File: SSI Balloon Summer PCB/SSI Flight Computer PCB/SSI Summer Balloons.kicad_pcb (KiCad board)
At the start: 4 copper layers, 77.5 x 61 mm, 111 parts, among them J1 Battery connector, J10 Conn_01x08, J2 Conn_01x02, J3 LoRa antenna, J5 SWDIO, J6 1040310811, J7 GPS antenna, J8 PT1000 Sensor, M1 MountingHole_3.2mm_M3, M2 MountingHole_3.2mm_M3, M3 MountingHole_3.2mm_M3, M4 MountingHole_3.2mm_M3, Q2 DMG2305UX-7, SW1 NRST, SW2 BOOT0, U11 TPS63070RNMR, U3 AP2112K-3.3TRG1, U7 STM32F411CEUx, Y1 ABM8W-12.0000MHZ-8-K1Z-T3

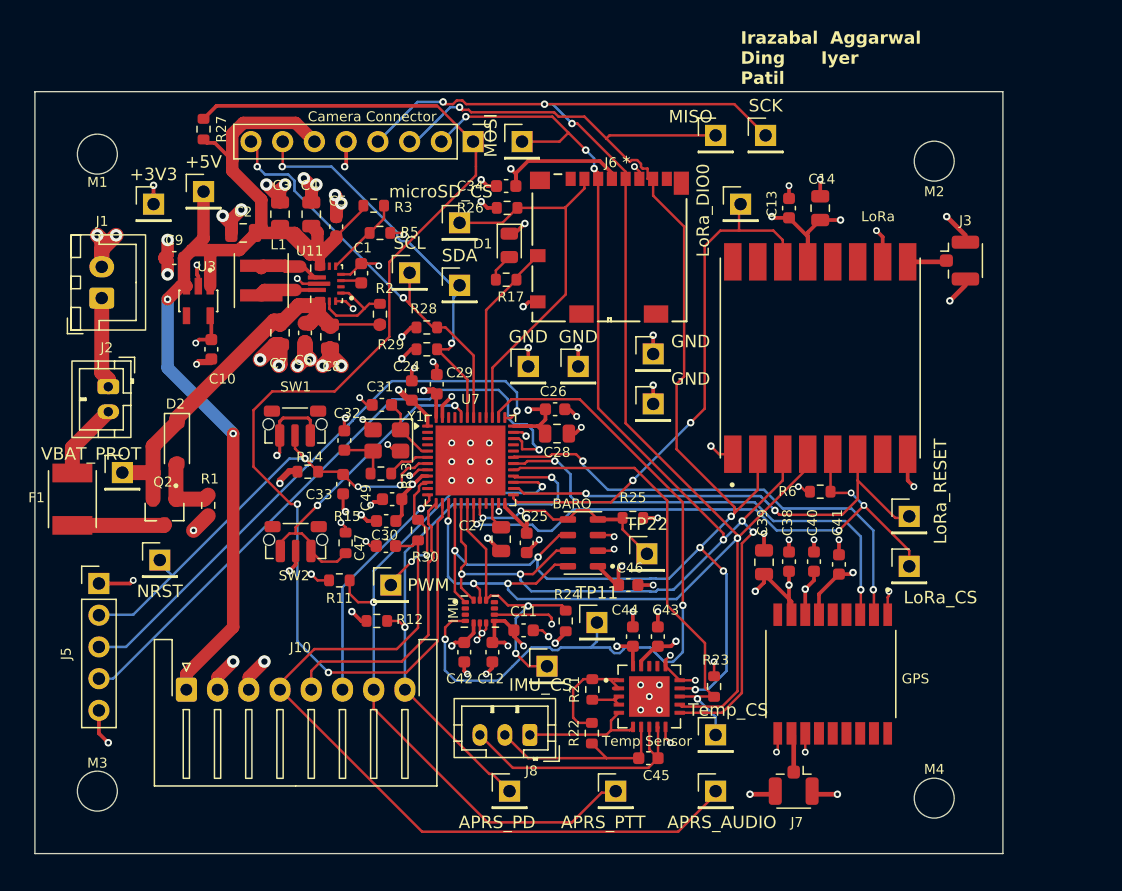
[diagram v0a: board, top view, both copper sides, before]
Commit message: Cleared space for microSD, organized SPI tracks
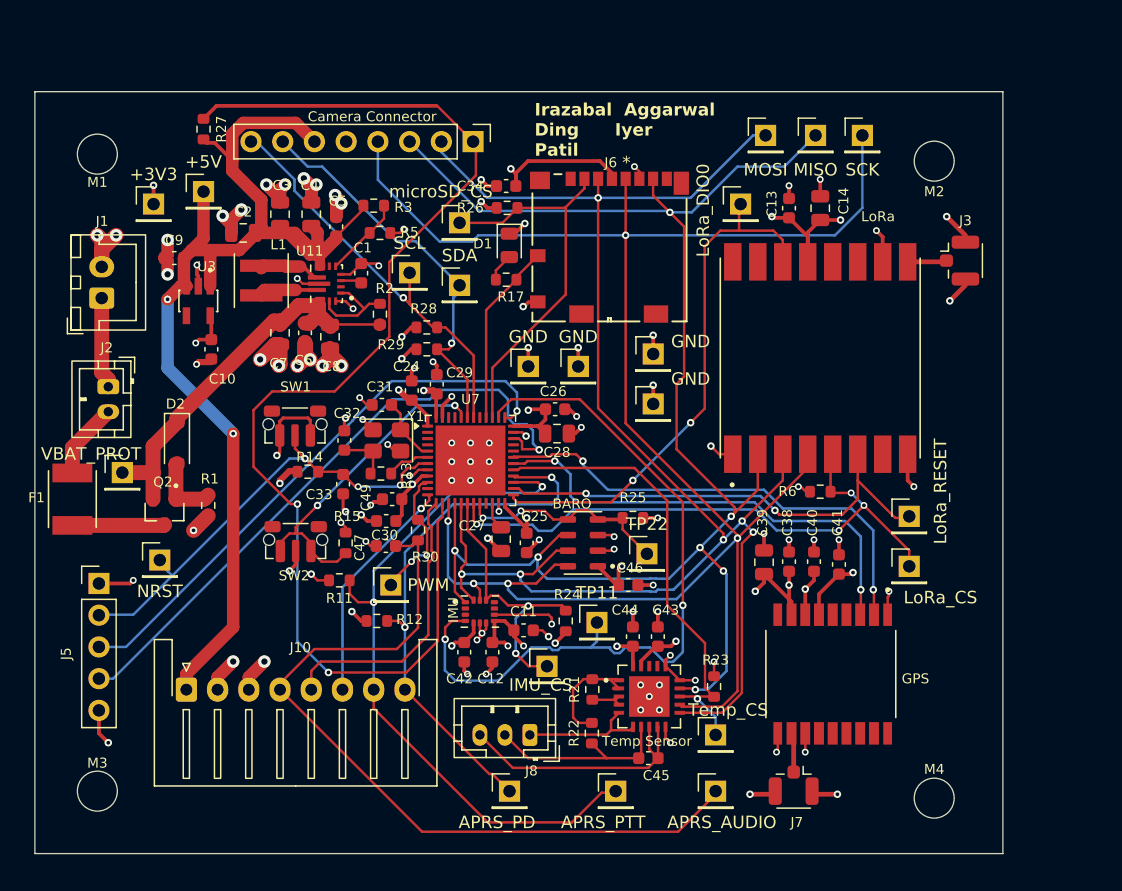
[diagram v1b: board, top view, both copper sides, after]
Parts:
- moved MOSI 19.5 mm to (158.5, 80.0)
- moved MISO 8.00 mm to (162.5, 80.0)
- moved SCK 7.75 mm to (166.2, 80.0)
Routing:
- net /MCU (STM)/MOSI: track 119.2 -> 129.0 mm, vias 8 -> 6
- net /MCU (STM)/SCK: track 141.1 -> 148.9 mm, vias 7 -> 5
- net /MCU (STM)/MISO: track 121.8 -> 126.5 mm
- net /MCU (STM)/SDA: track 35.2 -> 32.6 mm, vias 2 -> 1
- net GND: track 169.7 -> 167.9 mm, vias 100 -> 99
- net /MCU (STM)/SCL: track 34.2 -> 34.0 mm, vias 2 -> 1

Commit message: More silkscreen organization, combined some pinheaders
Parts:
- removed MISO, MOSI, SCK, SCL, SDA: Conn_01x01, Connector_PinHeader_2.54mm:PinHeader_1x01_P2.54mm_Vertical
- added J11: SPI, Connector_PinHeader_2.54mm:PinHeader_1x03_P2.54mm_Vertical, F.Cu at (164.8, 80.0)
- added J4: I2C, Connector_PinHeader_2.54mm:PinHeader_1x02_P2.54mm_Vertical, F.Cu at (130.5, 91.5)
- J1: value Battery connector -> BATT_CONN
- J9: renamed from Camera Connector; value Camera -> CAM_CONN
- TP1: renamed from +5V; value Conn_01x01 -> +5V
- TP10: renamed from NRST; value Conn_01x01 -> NRST
- TP11: value Conn_01x01 -> IMU_INT1
- TP12: renamed from LoRa_DIO0; value Conn_01x01 -> LoRa_DIO0
- TP13, TP3, TP5, TP8: renamed from GND; value Conn_01x01 -> GND
- TP14: renamed from APRS_PD; value Conn_01x01 -> APRS_PD
- TP15: renamed from APRS_PTT; value Conn_01x01 -> APRS_PT
- TP2: renamed from VBAT_PROT; value Conn_01x01 -> VBAT_PROT
- TP20: renamed from IMU_CS; value Conn_01x01 -> IMU_CS
- TP21: renamed from Temp_CS; value Conn_01x01 -> Temp_CS
- TP22: value Conn_01x01 -> BARO_CS
- TP23: renamed from LoRa_CS; value Conn_01x01 -> LoRa_CS
- TP24: renamed from microSD_CS; value Conn_01x01 -> microSD_CS
- TP25: renamed from LoRa_RESET; value Conn_01x01 -> LoRa_RESET
- TP4: renamed from +3V3; value Conn_01x01 -> +3V3
- TP6: renamed from APRS_AUDIO; value Conn_01x01 -> APRS_AUDIO
- TP7: renamed from PWM; value Conn_01x01 -> APRS_PWM
- U9: renamed from Temp Sensor
- moved TP1 1.35 mm to (113.0, 85.8)
- moved TP24 1.35 mm to (132.8, 87.5)
- moved TP2 1.12 mm to (106.5, 108.0)
- moved F1 0.50 mm to (102.5, 109.1)
- moved TP4 0.35 mm to (109.2, 85.8)
- renumbered LoRa to U1, BARO to U10, GPS to U8
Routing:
- net GND: track 167.9 -> 161.3 mm, vias 99 -> 95
- net +5V: track 92.3 -> 87.9 mm
- net +3V3: track 109.2 -> 104.8 mm, vias 33 -> 31
- net /MCU (STM)/SCK: track 148.9 -> 146.9 mm
- net /MCU (STM)/microSD_CS: track 31.2 -> 32.6 mm
- net /MCU (STM)/SDA: track 32.6 -> 33.9 mm
- net /MCU (STM)/MOSI: track 129.0 -> 130.3 mm
- net VBAT_PROT: track 32.7 -> 33.6 mm
- net /MCU (STM)/SCL: track 34.0 -> 34.9 mm, vias 1 -> 0
- net Net-(F1-Pad2): track 7.40 -> 7.90 mm

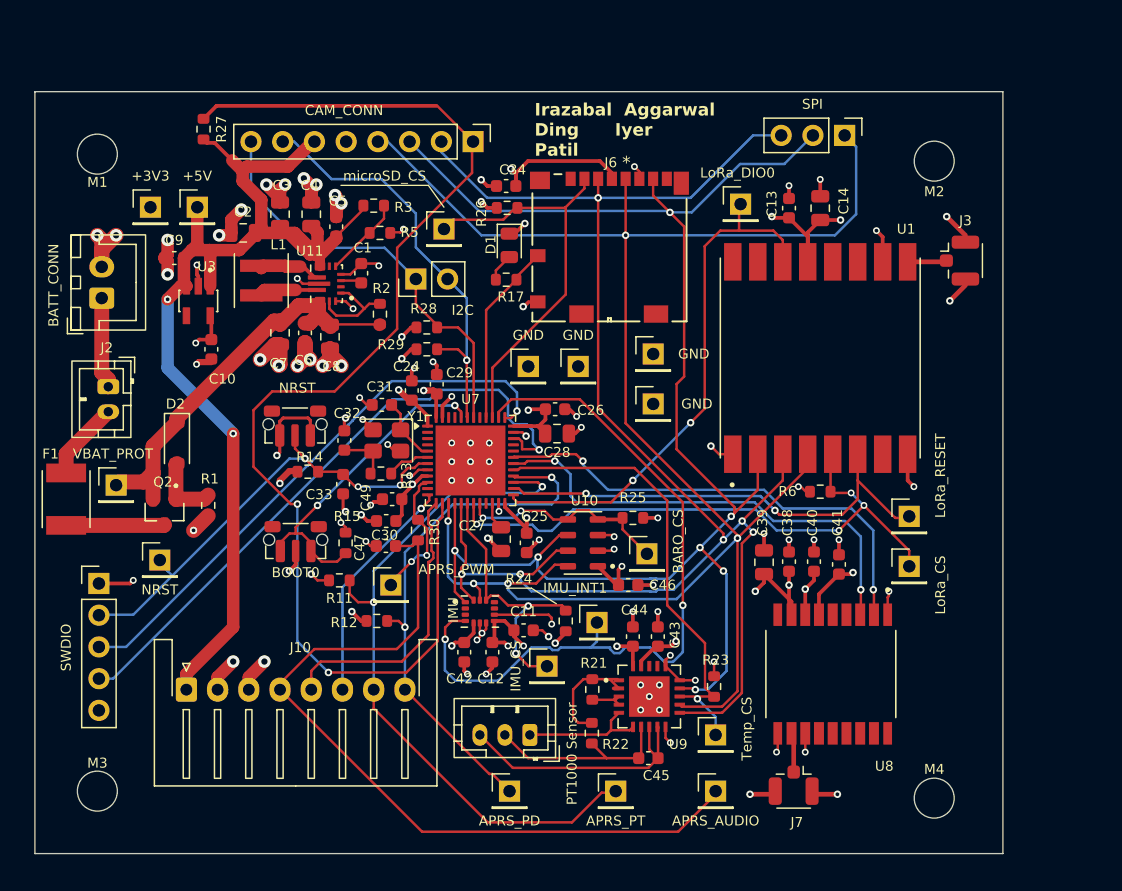
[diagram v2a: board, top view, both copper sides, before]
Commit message: Updated antenna connector
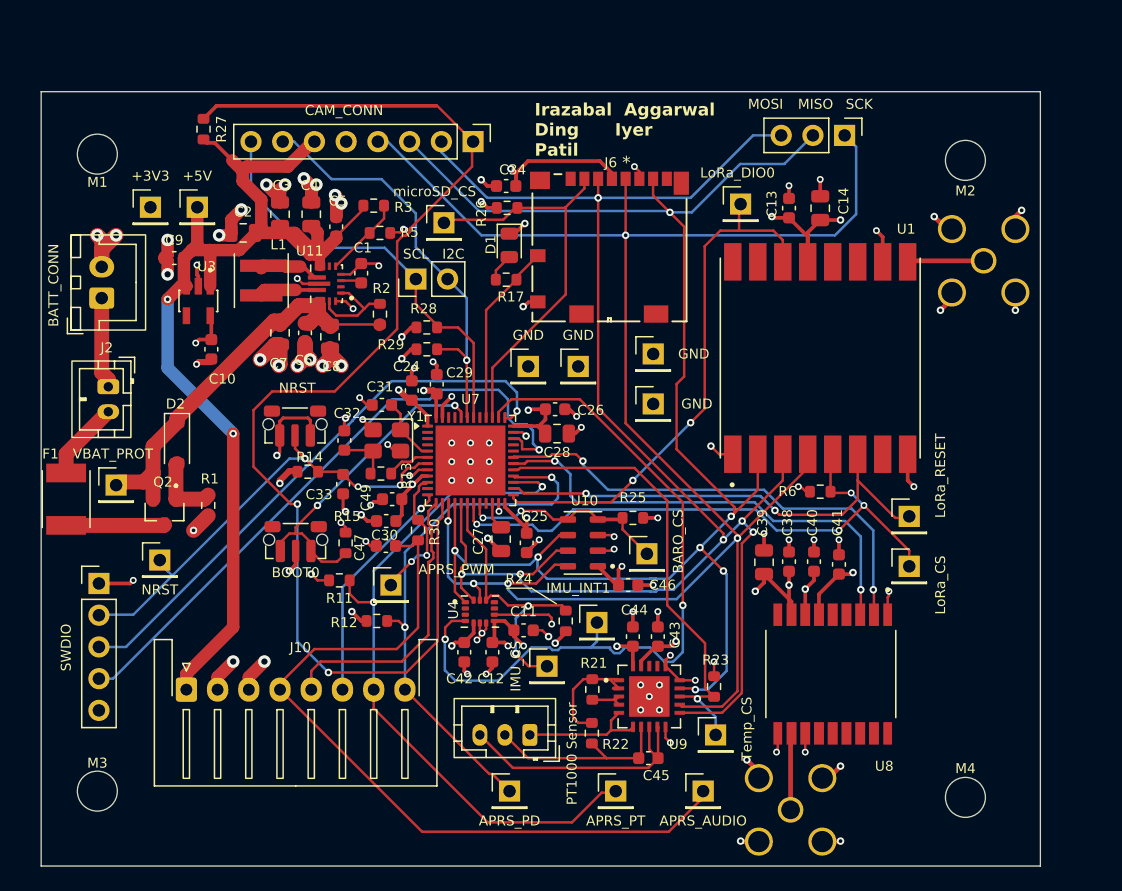
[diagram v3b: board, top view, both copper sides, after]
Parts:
- J3, J7: footprint Connector_Coaxial:U.FL_Hirose_U.FL-R-SMT-1_Vertical -> Connector_Coaxial:SMA_Amphenol_901-144_Vertical; moved to B.Cu
- moved M2 2.50 mm to (174.5, 82.0)
- moved M4 2.50 mm to (174.5, 133.0)
- moved J7 1.52 mm to (160.5, 134.0)
- moved J3 1.46 mm to (176.0, 90.0), turned to 180 degrees
- moved TP6 1.00 mm to (153.5, 132.5)
- moved TP24 0.50 mm to (132.8, 87.0)
- renumbered IMU to U4
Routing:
- net GND: track 161.3 -> 165.5 mm, vias 95 -> 99
- net Net-(J7-In): track 3.17 -> 6.40 mm
- net Net-(J3-In): track 3.14 -> 6.12 mm
- net /MCU (STM)/APRS_AUDIO: track 63.2 -> 62.5 mm
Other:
- board size 77.5 x 61 mm -> 80 x 62 mm
- board text added: "MISO"
- board text added: "MOSI"
- board text added: "SCK"
- board text added: "SCL"

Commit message: finished finding all parts on JLCPCB - finalizing BOM then order
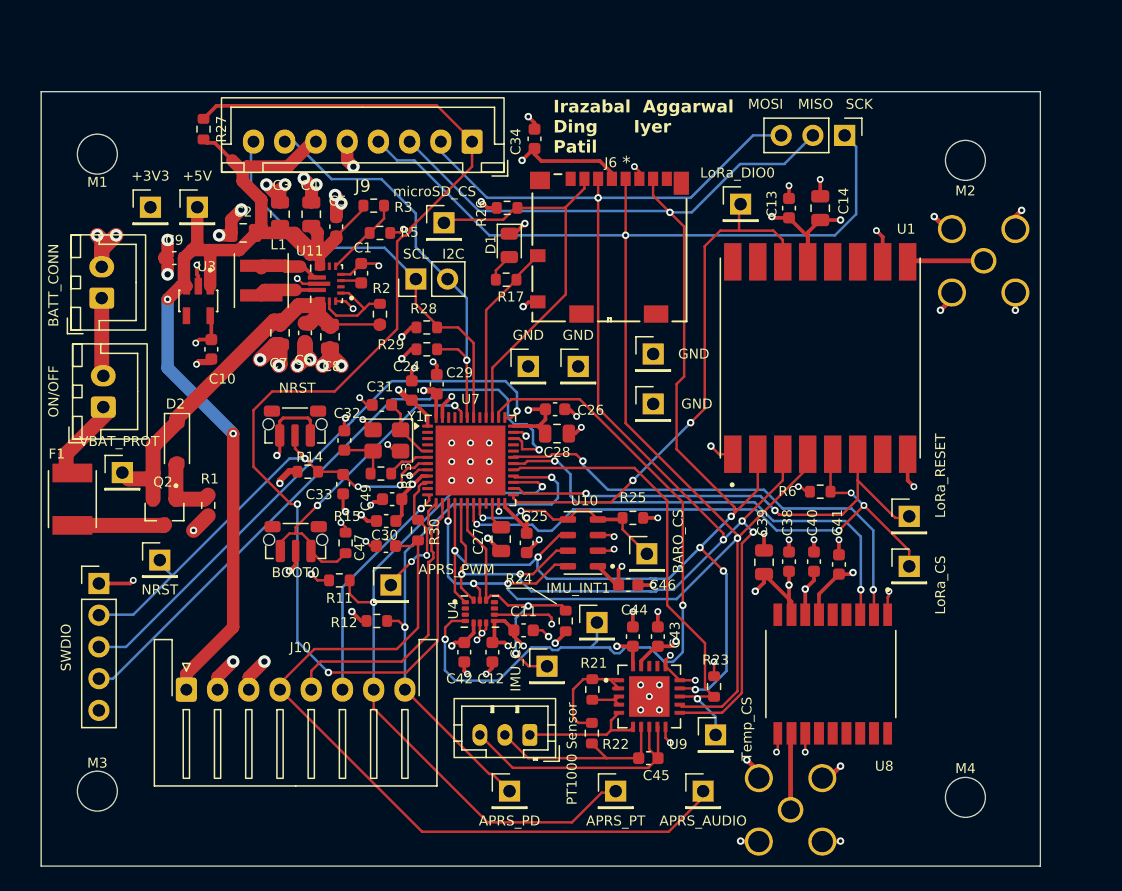
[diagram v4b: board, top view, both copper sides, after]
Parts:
- C1: value 100 nF -> 100nF
- C11, C33: value 0.1uF -> 100nF
- J2: footprint Connector_JST:JST_PH_B2B-PH-K_1x02_P2.00mm_Vertical -> Connector_JST:JST_XH_B2B-XH-A_1x02_P2.50mm_Vertical
- J9: footprint Connector_PinHeader_2.54mm:PinHeader_1x08_P2.54mm_Vertical -> Connector_JST:JST_XH_B8B-XH-A_1x08_P2.50mm_Vertical
- R17: value 330R -> 330
- moved C34 4.41 mm to (140.0, 80.3), turned to 90 degrees
- moved J2 1.67 mm to (105.5, 101.8), turned to 90 degrees
- moved TP2 1.12 mm to (107.0, 107.0)
- moved F1 0.50 mm to (103.0, 109.1)
- moved J9 0.08 mm to (135.0, 80.5), turned to 180 degrees
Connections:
- F1 pad 1: Net-(J2-Pin_2) -> Net-(J2-Pin_1)
- J2 pad 1: VBAT -> Net-(J2-Pin_1)
- J2 pad 2: Net-(J2-Pin_2) -> VBAT
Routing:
- net Net-(J2-Pin_1): track 0.00 -> 6.85 mm
- net Net-(J2-Pin_2): track 6.30 -> 0.00 mm
- net +3V3: track 104.8 -> 102.4 mm
- net GND: track 165.5 -> 167.5 mm, vias 99 -> 100
- net VBAT: track 7.32 -> 6.28 mm
- net /MCU (STM)/SDA: track 33.9 -> 34.9 mm
- net /MCU (STM)/SCK: track 146.9 -> 147.7 mm
- net VBAT_PROT: track 33.6 -> 32.9 mm
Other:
- board text added: "ON/OFF"

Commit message: PCB finally done i think and ready to order
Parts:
- removed R17: 330, Resistor_SMD:R_0603_1608Metric
- added C35: 1uF, Capacitor_SMD:C_0603_1608Metric, F.Cu at (153.0, 81.0)
- added R18: 330, Resistor_SMD:R_0603_1608Metric, F.Cu at (137.3, 93.3)
- added R31: 1k, Resistor_SMD:R_0603_1608Metric, F.Cu at (139.5, 118.0)
- R13: value R_EXT -> 0
- moved C34 1.24 mm to (139.0, 81.0)
- moved D1 1.13 mm to (137.5, 89.8)
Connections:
- U4 pad 9: GND -> Net-(U4-INT2/FSYNC/CLKIN)
- U7 pad 41: unconnected-(U7-PB5-Pad41) -> Net-(U7-PB5)
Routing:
- net Net-(U7-PB5): track 0.00 -> 9.18 mm
- net +3V3: track 102.4 -> 111.4 mm, vias 31 -> 32
- net GND: track 167.5 -> 164.4 mm, vias 100 -> 101
- net /MCU (STM)/IMU_CS: track 22.7 -> 25.0 mm
- net Net-(U4-INT2/FSYNC/CLKIN): track 0.00 -> 2.04 mm

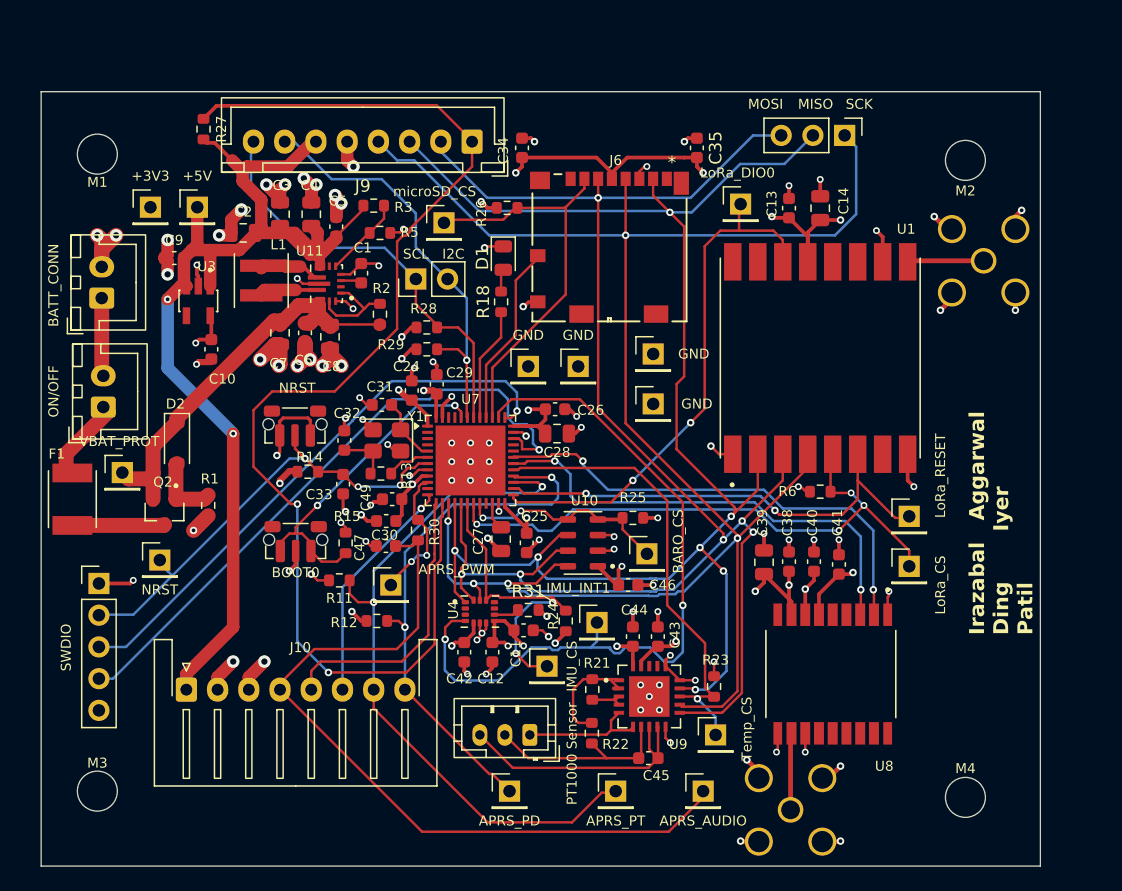
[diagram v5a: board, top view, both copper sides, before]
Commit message: Board done but we have a price crisis so might have to change things
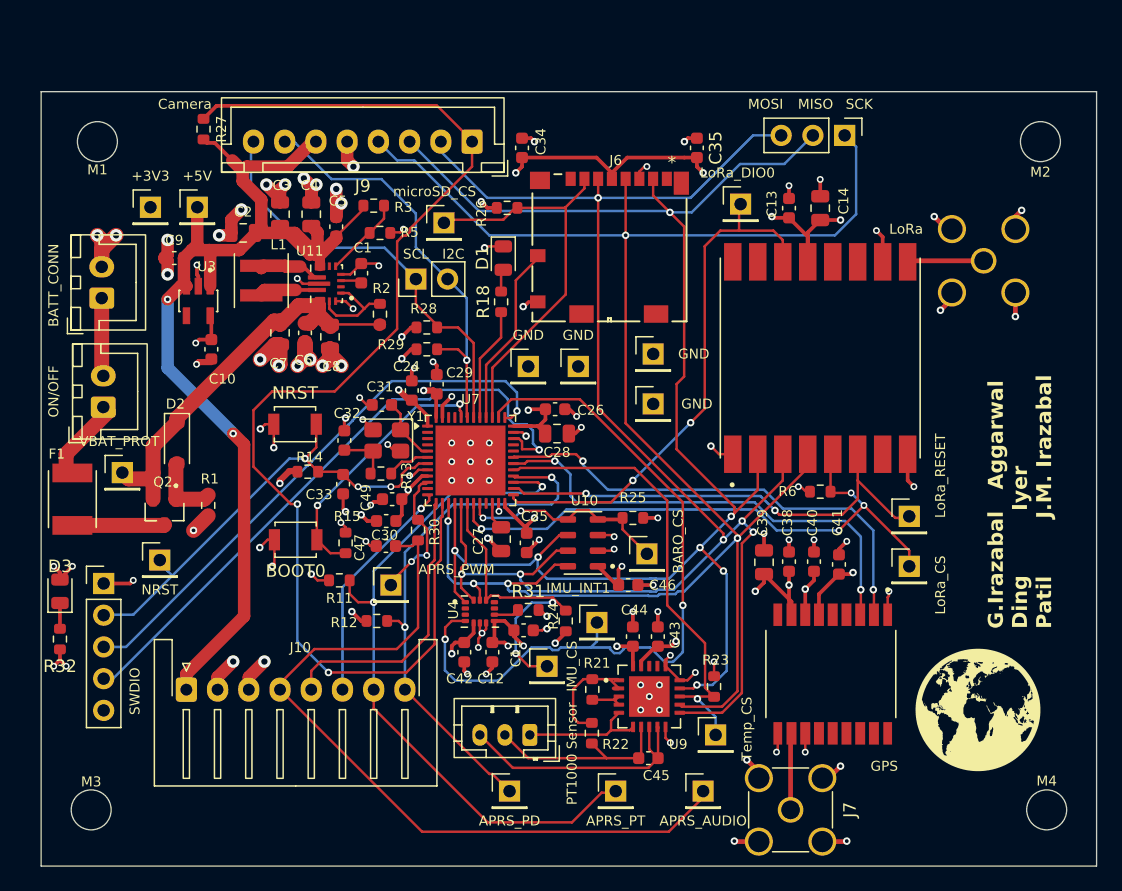
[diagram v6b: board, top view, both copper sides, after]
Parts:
- added D3: LED, LED_SMD:LED_0805_2012Metric, F.Cu at (102.0, 116.5)
- added G***: LOGO, LOGO, F.Cu at (175.5, 126.0)
- added R32: 1k, Resistor_SMD:R_0603_1608Metric, F.Cu at (102.0, 120.3)
- BOOT0: renamed from SW2; footprint Button_Switch_SMD:SW_Push_1P1T-MP_NO_Horizontal_Alps_SKRTLAE010 -> Button_Switch_SMD:SW_SPST_B3U-1000P
- J7: moved to F.Cu
- NRST: renamed from SW1; footprint Button_Switch_SMD:SW_Push_1P1T-MP_NO_Horizontal_Alps_SKRTLAE010 -> Button_Switch_SMD:SW_SPST_B3U-1000P
- R18: value 330 -> 150
- moved M4 6.58 mm to (181.0, 134.0)
- moved M2 6.19 mm to (180.5, 80.5)
- moved M3 1.58 mm to (104.5, 134.0)
- moved M1 1.00 mm to (105.0, 80.5)
- moved J5 0.38 mm to (105.5, 115.9)
- turned NRST to 0 degrees
- renumbered U8 to GPS, U1 to LoRa
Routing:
- net +3V3: track 111.4 -> 117.0 mm, vias 32 -> 35
- net /MCU (STM)/BOOT0: track 26.3 -> 21.4 mm
- net Net-(D3-K): track 0.00 -> 2.06 mm
- net GND: track 164.4 -> 165.7 mm, vias 101 -> 104
- net /MCU (STM)/NRST: track 37.8 -> 38.8 mm
- net +5V: track 87.9 -> 88.6 mm
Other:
- board size 80 x 62 mm -> 84.5 x 62 mm
- board text added: "Camera"
- board text added: "G.Irazabal Aggarwal Ding Iyer Patil J.M. Irazabal"
- board text removed: "Irazabal Aggarwal Ding Iyer Patil"
